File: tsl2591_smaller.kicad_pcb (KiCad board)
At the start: 2 copper layers, 14 x 14 mm, 7 parts, among them J1 Conn_01x04_Female, Q1 BSS138, Q2 BSS138, U1 TSL2591

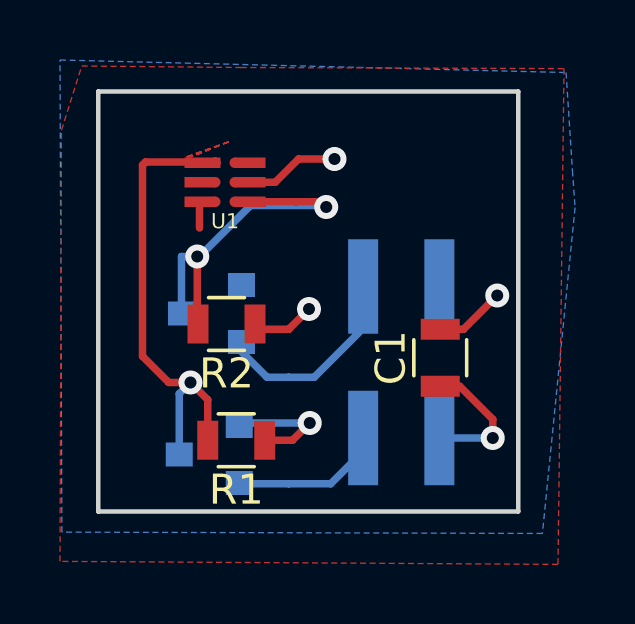
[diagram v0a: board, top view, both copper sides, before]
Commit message: Removed more components
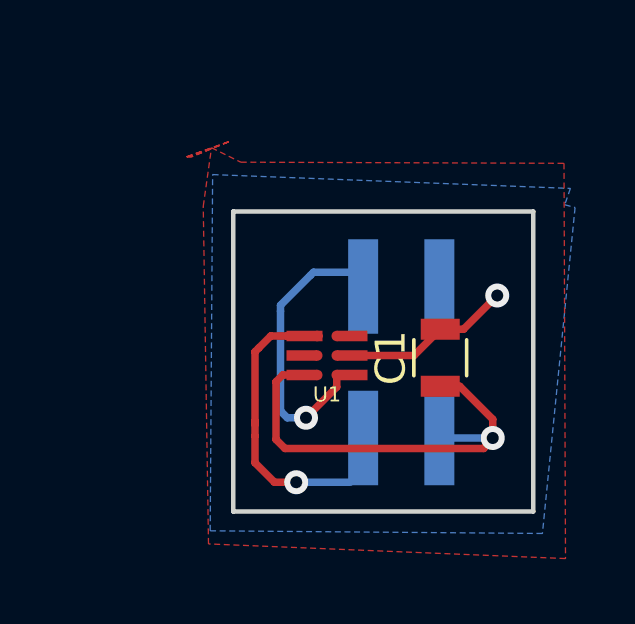
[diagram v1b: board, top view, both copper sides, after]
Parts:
- removed Q1, Q2: BSS138, TO_SOT_Packages_SMD:SOT-23
- removed R1, R2: 10k, Resistors_SMD:R_0805
- moved U1 6.70 mm to (185.7, 84.9)
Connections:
- U1 pad 1: /SCL_out -> /SCL_in
- U1 pad 6: /SDA_out -> /SDA_in
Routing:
- net /SCL_out: track 14.4 -> 0.00 mm, vias 1 -> 0
- net /SDA_out: track 12.3 -> 0.00 mm, vias 2 -> 0
- net GND: track 6.62 -> 15.5 mm
- net /SCL_in: track 4.90 -> 11.0 mm, vias 0 -> 1
- net +3V3: track 11.9 -> 6.04 mm, vias 4 -> 1
- net /SDA_in: track 5.04 -> 9.50 mm, vias 0 -> 1
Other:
- board size 14 x 14 mm -> 10 x 10 mm
